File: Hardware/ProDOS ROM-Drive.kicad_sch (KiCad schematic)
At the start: 17 parts, among them J1 Apple II Expansion Slot, U1 74LS00, U2 74LS32

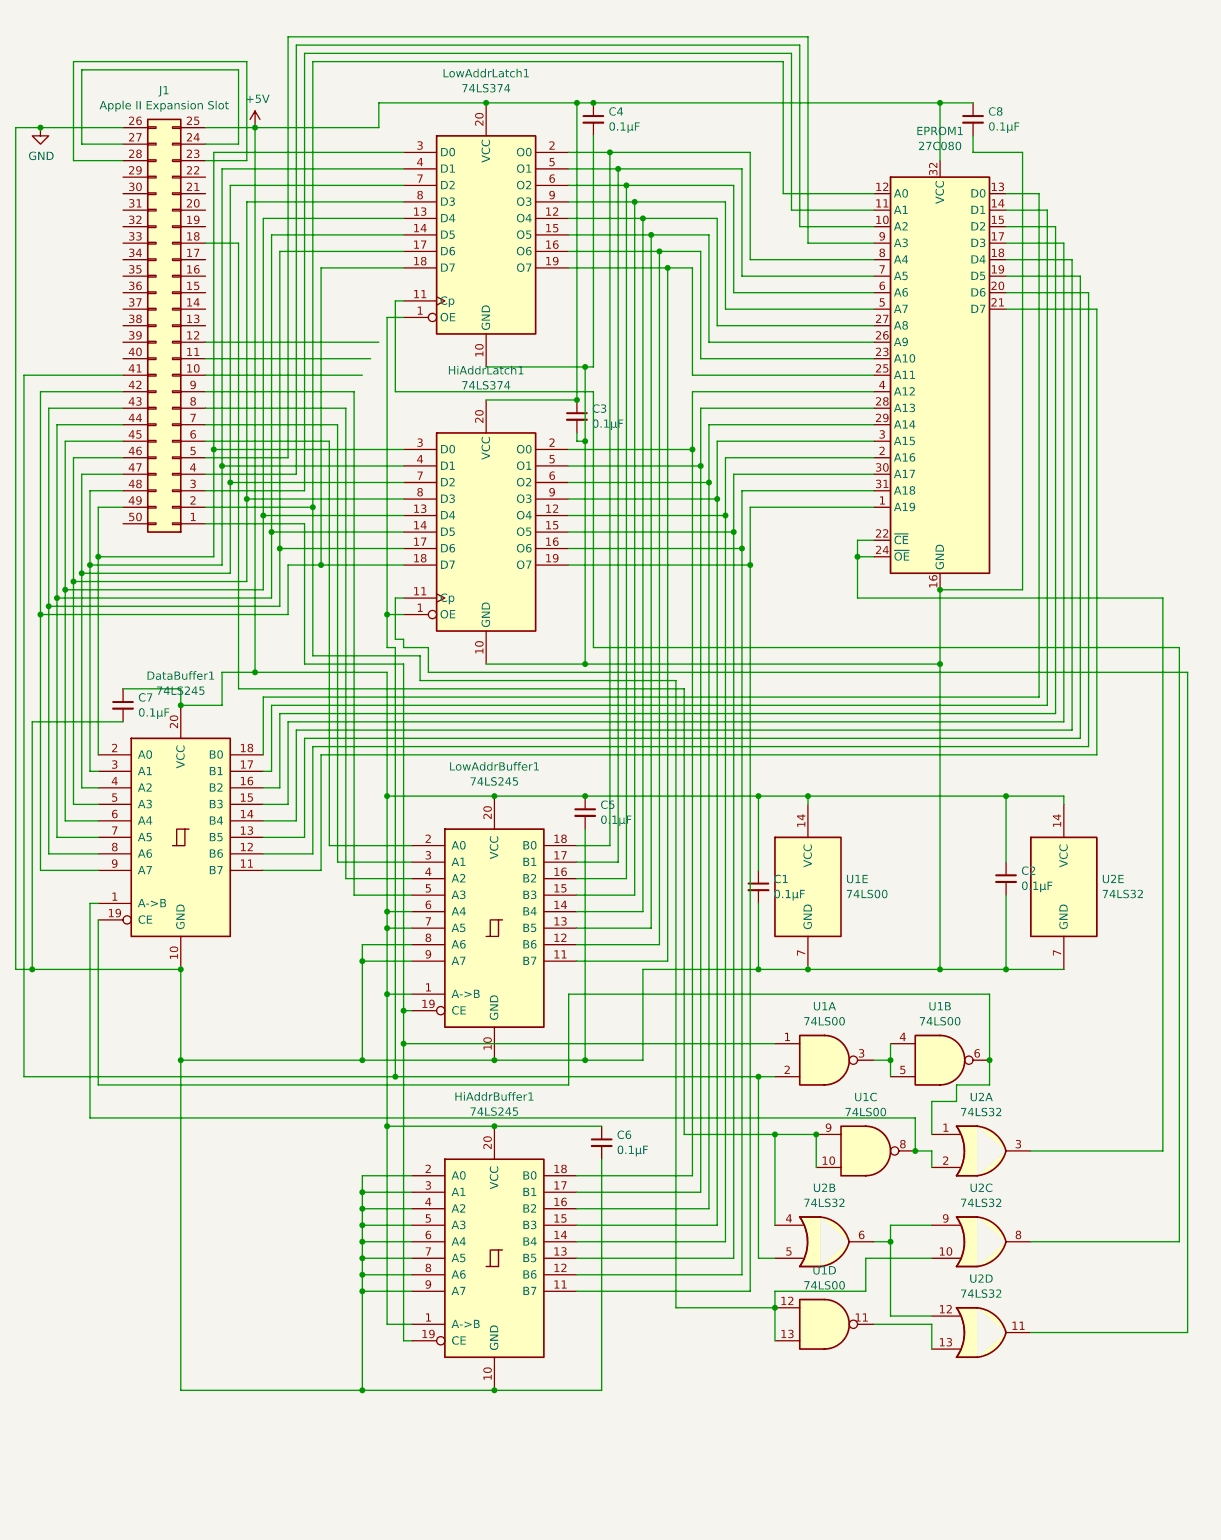
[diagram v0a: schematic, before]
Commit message: Update schematic and fix data bus lines
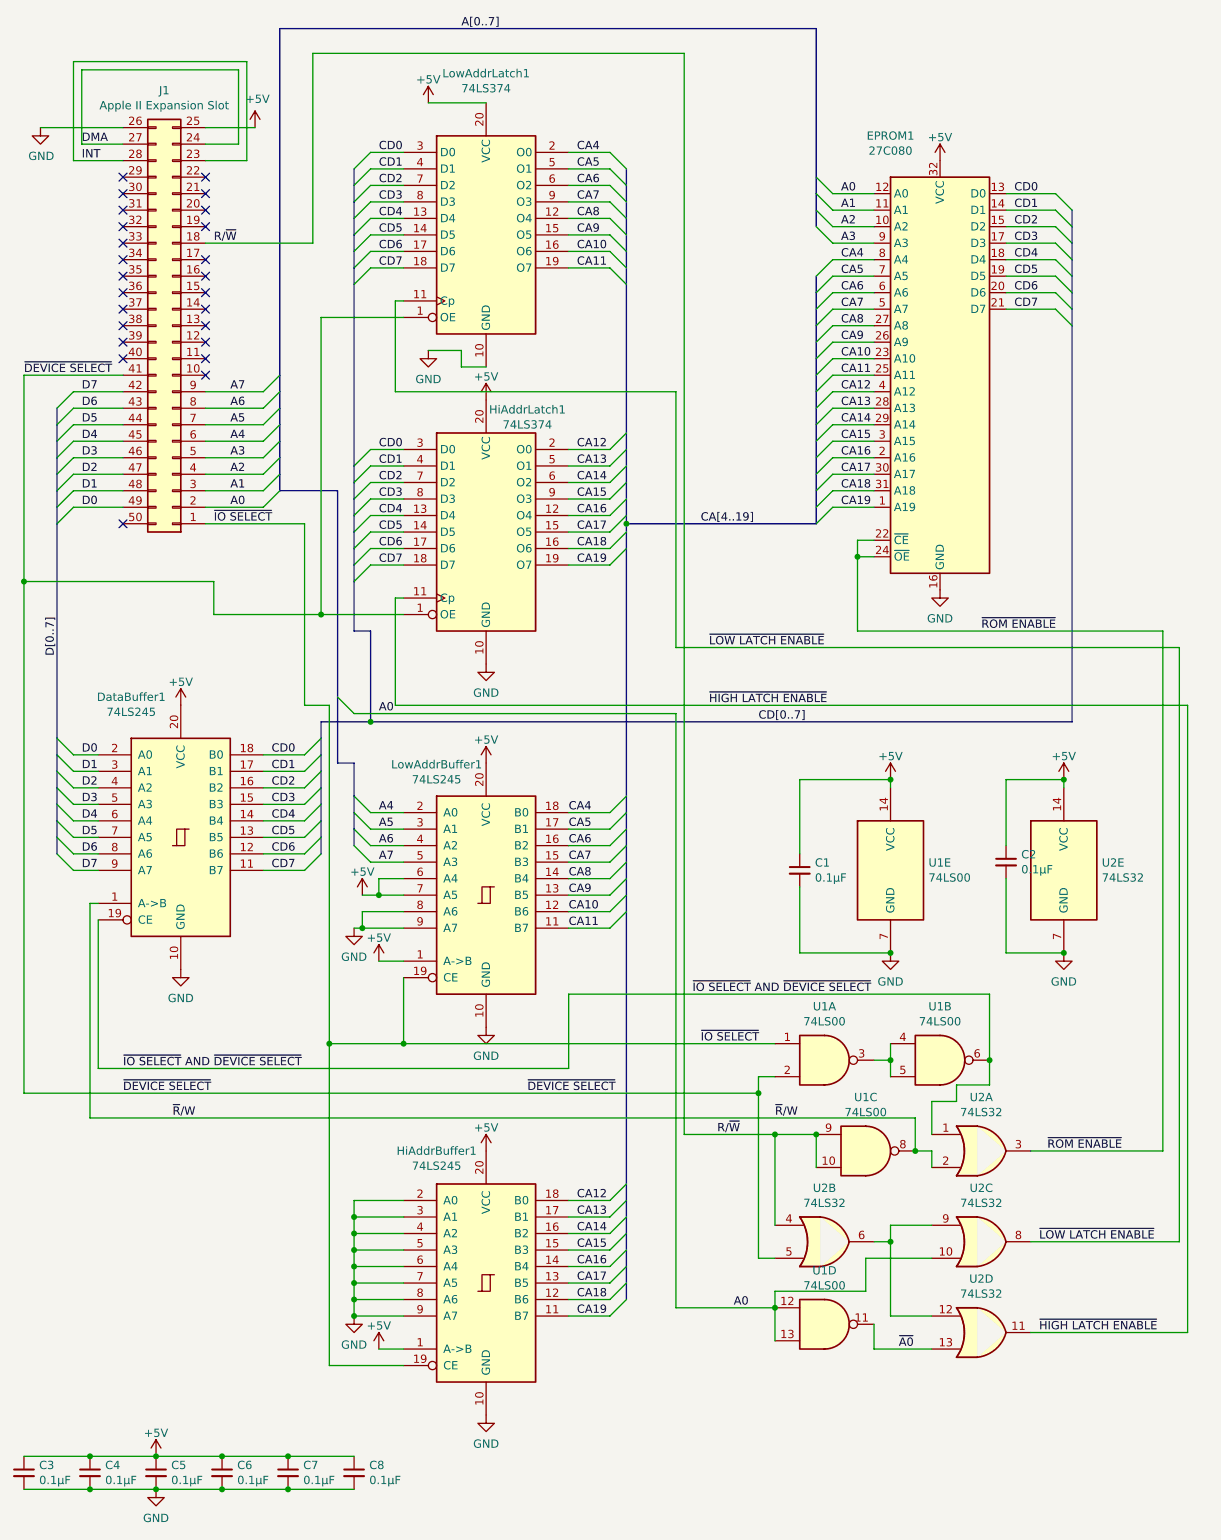
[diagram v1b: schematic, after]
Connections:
- net ~{IO SELECT}: now reaches HiAddrBuffer1.19 (CE), J1.1 (Pin_1), LowAddrBuffer1.19 (CE), U1.1
- net R/~{W}: now reaches J1.18 (Pin_18), U1.10, U1.9, U2.4
- net A0: now reaches EPROM1.12 (A0), J1.2 (Pin_2), U1.12, U1.13, U2.10
- net INT: now reaches J1.23 (Pin_23), J1.28 (Pin_28)
- net DMA: now reaches J1.24 (Pin_24), J1.27 (Pin_27)
- net A1: now reaches EPROM1.11 (A1), J1.3 (Pin_3)
- net A2: now reaches EPROM1.10 (A2), J1.4 (Pin_4)
- net ~{DEVICE SELECT}: now reaches HiAddrLatch1.1 (OE), J1.41 (Pin_41), LowAddrLatch1.1 (OE), U1.2, U2.5
- net CD7: now reaches HiAddrLatch1.18 (D7), LowAddrLatch1.18 (D7)
- net CD7: now also DataBuffer1.11 (B7), EPROM1.21 (D7); no longer DataBuffer1.9 (A7), J1.42 (Pin_42)
- net CD6: now reaches HiAddrLatch1.17 (D6), LowAddrLatch1.17 (D6)
- net CD6: now also DataBuffer1.12 (B6), EPROM1.20 (D6); no longer DataBuffer1.8 (A6), J1.43 (Pin_43)
- net CD5: now reaches HiAddrLatch1.14 (D5), LowAddrLatch1.14 (D5)
- net CD5: now also DataBuffer1.13 (B5), EPROM1.19 (D5); no longer DataBuffer1.7 (A5), J1.44 (Pin_44)
- net CD4: now reaches HiAddrLatch1.13 (D4), LowAddrLatch1.13 (D4)
- net CD4: now also DataBuffer1.14 (B4), EPROM1.18 (D4); no longer DataBuffer1.6 (A4), J1.45 (Pin_45)
- net CD3: now reaches HiAddrLatch1.8 (D3), LowAddrLatch1.8 (D3)
- net CD3: now also DataBuffer1.15 (B3), EPROM1.17 (D3); no longer DataBuffer1.5 (A3), J1.46 (Pin_46)
- net CD2: now reaches HiAddrLatch1.7 (D2), LowAddrLatch1.7 (D2)
- net CD2: now also DataBuffer1.16 (B2), EPROM1.15 (D2); no longer DataBuffer1.4 (A2), J1.47 (Pin_47)
- net CD1: now reaches HiAddrLatch1.4 (D1), LowAddrLatch1.4 (D1)
- net CD1: now also DataBuffer1.17 (B1), EPROM1.14 (D1); no longer DataBuffer1.3 (A1), J1.48 (Pin_48)
- net CD0: now reaches HiAddrLatch1.3 (D0), LowAddrLatch1.3 (D0)
- net CD0: now also DataBuffer1.18 (B0), EPROM1.13 (D0); no longer DataBuffer1.2 (A0), J1.49 (Pin_49)
- net A3: now reaches EPROM1.9 (A3), J1.5 (Pin_5)
- net A4: now reaches J1.6 (Pin_6), LowAddrBuffer1.2 (A0)
- net A5: now reaches J1.7 (Pin_7), LowAddrBuffer1.3 (A1)
- net A6: now reaches J1.8 (Pin_8), LowAddrBuffer1.4 (A2)
- net A7: now reaches J1.9 (Pin_9), LowAddrBuffer1.5 (A3)
- net ~{IO SELECT} AND ~{DEVICE SELECT}: now reaches DataBuffer1.19 (CE), U1.6, U2.1
- net ~{R}/W: now reaches DataBuffer1.1 (A->B), U1.8, U2.2
- net ~{A0}: now reaches U1.11, U2.13
- net ~{ROM ENABLE}: now reaches EPROM1.22 (~{CE}), EPROM1.24 (~{OE}), U2.3
- net ~{LOW LATCH ENABLE}: now reaches LowAddrLatch1.11 (Cp), U2.8
- net ~{HIGH LATCH ENABLE}: now reaches HiAddrLatch1.11 (Cp), U2.11
- net CA11: now reaches EPROM1.25 (A11), LowAddrBuffer1.11 (B7), LowAddrLatch1.19 (O7)
- net CA10: now reaches EPROM1.23 (A10), LowAddrBuffer1.12 (B6), LowAddrLatch1.16 (O6)
- net CA9: now reaches EPROM1.26 (A9), LowAddrBuffer1.13 (B5), LowAddrLatch1.15 (O5)
- net CA8: now reaches EPROM1.27 (A8), LowAddrBuffer1.14 (B4), LowAddrLatch1.12 (O4)
- net CA7: now reaches EPROM1.5 (A7), LowAddrBuffer1.15 (B3), LowAddrLatch1.9 (O3)
- net CA6: now reaches EPROM1.6 (A6), LowAddrBuffer1.16 (B2), LowAddrLatch1.6 (O2)
- net CA5: now reaches EPROM1.7 (A5), LowAddrBuffer1.17 (B1), LowAddrLatch1.5 (O1)
- net CA4: now reaches EPROM1.8 (A4), LowAddrBuffer1.18 (B0), LowAddrLatch1.2 (O0)
- net CA19: now reaches EPROM1.1 (A19), HiAddrBuffer1.11 (B7), HiAddrLatch1.19 (O7)
- net CA18: now reaches EPROM1.31 (A18), HiAddrBuffer1.12 (B6), HiAddrLatch1.16 (O6)
- net CA17: now reaches EPROM1.30 (A17), HiAddrBuffer1.13 (B5), HiAddrLatch1.15 (O5)
- net CA16: now reaches EPROM1.2 (A16), HiAddrBuffer1.14 (B4), HiAddrLatch1.12 (O4)
- net CA15: now reaches EPROM1.3 (A15), HiAddrBuffer1.15 (B3), HiAddrLatch1.9 (O3)
- net CA14: now reaches EPROM1.29 (A14), HiAddrBuffer1.16 (B2), HiAddrLatch1.6 (O2)
- net CA13: now reaches EPROM1.28 (A13), HiAddrBuffer1.17 (B1), HiAddrLatch1.5 (O1)
- net CA12: now reaches EPROM1.4 (A12), HiAddrBuffer1.18 (B0), HiAddrLatch1.2 (O0)
- new net D0: DataBuffer1.2 (A0), J1.49 (Pin_49)
- new net D1: DataBuffer1.3 (A1), J1.48 (Pin_48)
- new net D2: DataBuffer1.4 (A2), J1.47 (Pin_47)
- new net D3: DataBuffer1.5 (A3), J1.46 (Pin_46)
- new net D4: DataBuffer1.6 (A4), J1.45 (Pin_45)
- new net D5: DataBuffer1.7 (A5), J1.44 (Pin_44)
- new net D6: DataBuffer1.8 (A6), J1.43 (Pin_43)
- new net D7: DataBuffer1.9 (A7), J1.42 (Pin_42)
- no-connect marks 0 -> 25
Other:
- moved on the sheet: C1, C2, C3, C4, C5, C6, C7, C8, HiAddrBuffer1, LowAddrBuffer1, U1E, U2E
